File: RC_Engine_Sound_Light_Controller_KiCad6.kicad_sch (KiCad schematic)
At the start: 40 parts, among them J1 RX, J10 RGB, J11 32, J12 CH1, J13 CH2, J14 CH3, J15 ESC, J16 CH4, J2 HeadL, J3 TailL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

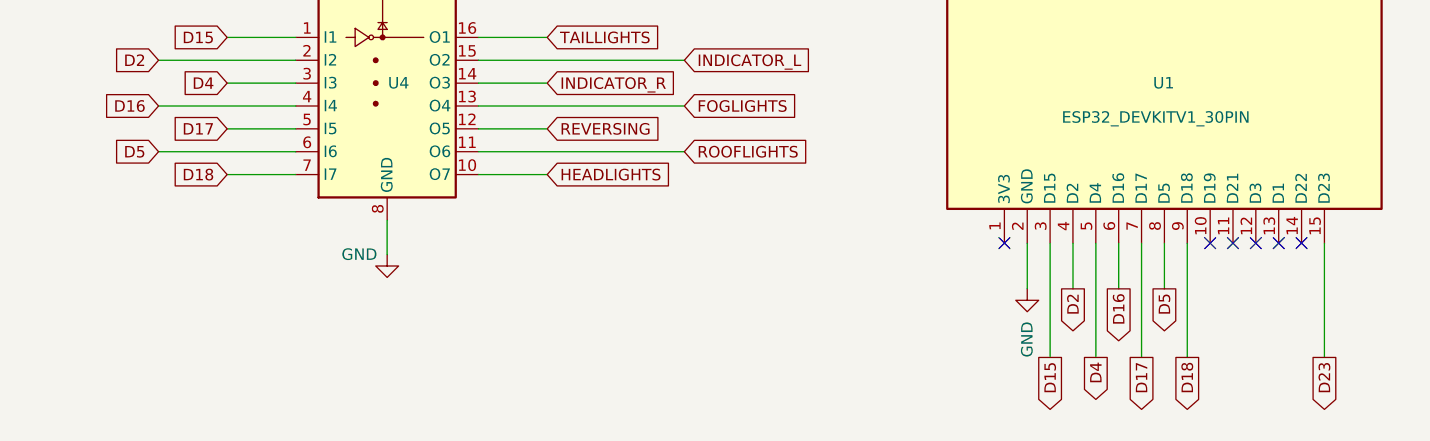
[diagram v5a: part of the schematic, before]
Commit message: Fixed wrong headlight pin (moved from D18 to D3).
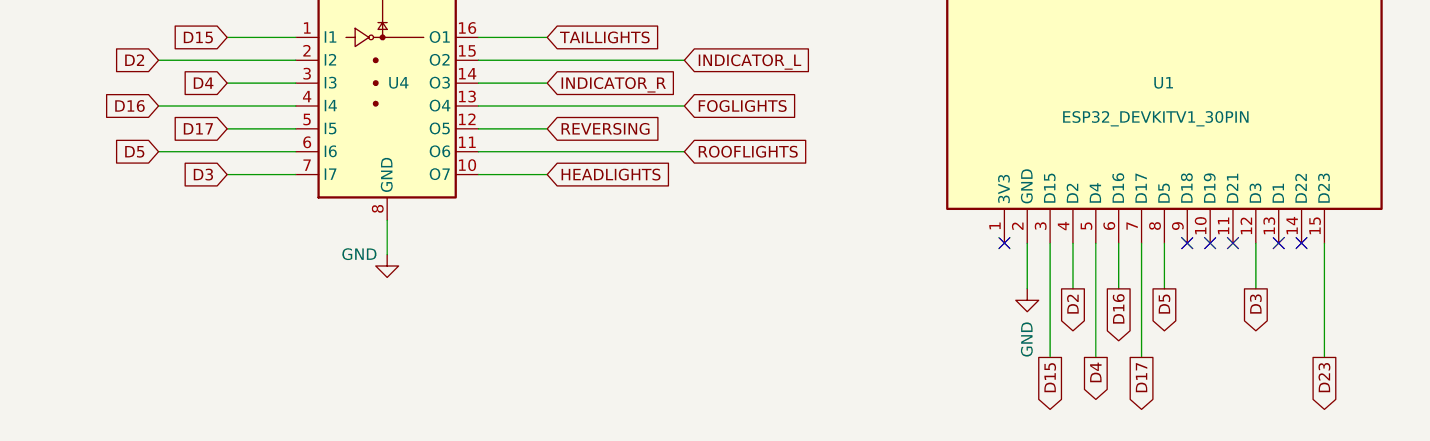
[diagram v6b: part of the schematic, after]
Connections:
- net D3: now reaches U1.12 (D3)
- net D3: now also U4.7 (I7)
- net D18: no longer names the net of U1.9 (D18)
- net D18: no longer U4.7 (I7)
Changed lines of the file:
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@@
   )
   (no_connect (at 149.86 133.35))
+  (no_connect (at 144.78 168.91))
   (no_connect (at 149.86 168.91))
-  (no_connect (at 152.4 168.91))
   (no_connect (at 154.94 168.91))
   (no_connect (at 157.48 168.91))
@@
     (stroke (width 0) (type default) (color 0 0 0 0))
   )
-  (wire (pts (xy 144.78 168.91) (xy 144.78 181.61))
+  (wire (pts (xy 152.4 168.91) (xy 152.4 173.99))
     (stroke (width 0) (type default) (color 0 0 0 0))
   )
@@
     )
   )
-  (global_label "D18" (shape output) (at 144.78 181.61 270) (fields_autoplaced)
-    (effects (font (size 1.27 1.27)) (justify right))
-    (property "Intersheet References" "${INTERSHEET_REFS}" (id 0) (at 144.7006 187.7121 90)
+  (global_label "D3" (shape output) (at 152.4 173.99 270) (fields_autoplaced)
+    (effects (font (size 1.27 1.27)) (justify right))
+    (property "Intersheet References" "${INTERSHEET_REFS}" (id 0) (at 152.3206 178.8826 90)
       (effects (font (size 1.27 1.27)) (justify right) hide)
     )
@@
     )
   )
-  (global_label "D18" (shape input) (at 38.1 161.29 180) (fields_autoplaced)
-    (effects (font (size 1.27 1.27)) (justify right))
-    (property "Intersheet References" "${INTERSHEET_REFS}" (id 0) (at 31.9979 161.2106 0)
-      (effects (font (size 1.27 1.27)) (justify right) hide)
-    )
+  (global_label "D3" (shape input) (at 38.1 161.29 180) (fields_autoplaced)
+    (effects (font (size 1.27 1.27)) (justify right))
+    (property "Intersheet References" "${INTERSHEET_REFS}" (id 0) (at 33.2074 161.2106 0)
+      (effects (font (size 1.27 1.27)) (justify right) hide)
+    )
